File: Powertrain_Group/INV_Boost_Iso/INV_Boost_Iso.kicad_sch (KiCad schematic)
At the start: 16 parts, among them J1 15230682601000, U27 TPS22917DBV

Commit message: [INV_Bost_Isense] V1.1
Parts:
- C41, C42, C43, C44, C45, C46: footprint Personal:C_8060_Murata_DK1 -> nturt_kicad_lib_EP7:C_8060_Murata_DK1
- J1: footprint Samacsys:15230682601000 -> nturt_kicad_lib_EP7:HARTING 15230682601000; symbol Samacsys:15230682601000 -> nturt_kicad_lib_EP7:Harting_15230682601000
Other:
- note added: "V1.0 init by Shinkansen942 V1.1 minor modify by Jack Kuo"
- company: (none) -> NTURacing
- title: (none) -> INV_Boost_Iso
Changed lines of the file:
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@@
 	(generator_version "9.0")
 	(paper "A4")
+	(title_block
+		(title "INV_Boost_Iso")
+		(date "2026-03-06")
+		(rev "1.1")
+		(company "NTURacing")
+		(comment 1 "Shinkansen942")
+		(comment 2 "Jack Kuo")
+	)
+	(text "V1.0 init by Shinkansen942\nV1.1 minor modify by Jack Kuo"
+		(exclude_from_sim no)
+		(at 192.786 92.71 0)
+		(effects
+			(font
+				(size 1.27 1.27)
+			)
+			(justify left top)
+		)
+	)
 	(junction
 		(at 104.14 73.66)
@@
 	)
 	(junction
-		(at 115.57 142.24)
+		(at 121.92 29.21)
 		(diameter 0)
 		(color 0 0 0 0)
 	)
 	(junction
-		(at 121.92 29.21)
+		(at 111.76 139.7)
 		(diameter 0)
 		(color 0 0 0 0)
@@
 	)
 	(junction
-		(at 140.97 134.62)
+		(at 109.22 60.96)
 		(diameter 0)
 		(color 0 0 0 0)
 	)
 	(junction
-		(at 109.22 60.96)
+		(at 48.26 53.34)
 		(diameter 0)
 		(color 0 0 0 0)
 	)
 	(junction
-		(at 48.26 53.34)
+		(at 158.75 73.66)
 		(diameter 0)
 		(color 0 0 0 0)
 	)
 	(junction
-		(at 158.75 73.66)
+		(at 111.76 142.24)
 		(diameter 0)
 		(color 0 0 0 0)
@@
 	)
 	(junction
-		(at 153.67 66.04)
+		(at 143.51 132.08)
 		(diameter 0)
 		(color 0 0 0 0)
 	)
 	(junction
-		(at 140.97 139.7)
+		(at 153.67 66.04)
 		(diameter 0)
 		(color 0 0 0 0)
 	)
 	(junction
-		(at 109.22 63.5)
+		(at 143.51 137.16)
 		(diameter 0)
 		(color 0 0 0 0)
 	)
 	(junction
-		(at 109.22 66.04)
+		(at 143.51 134.62)
 		(diameter 0)
 		(color 0 0 0 0)
 	)
 	(junction
-		(at 140.97 137.16)
+		(at 109.22 63.5)
 		(diameter 0)
 		(color 0 0 0 0)
 	)
 	(junction
-		(at 115.57 139.7)
+		(at 143.51 139.7)
 		(diameter 0)
 		(color 0 0 0 0)
 	)
 	(junction
-		(at 153.67 60.96)
+		(at 109.22 66.04)
 		(diameter 0)
 		(color 0 0 0 0)
 	)
 	(junction
-		(at 140.97 132.08)
+		(at 153.67 60.96)
 		(diameter 0)
 		(color 0 0 0 0)
@@
 	(wire
 		(pts
-			(xy 82.55 29.21) (xy 99.06 29.21)
+			(xy 143.51 139.7) (xy 140.97 139.7)
 		)
 		(stroke
@@
 	(wire
 		(pts
-			(xy 115.57 139.7) (xy 115.57 142.24)
+			(xy 82.55 29.21) (xy 99.06 29.21)
 		)
 		(stroke
@@
 	(wire
 		(pts
-			(xy 104.14 73.66) (xy 115.57 73.66)
+			(xy 143.51 134.62) (xy 143.51 137.16)
 		)
 		(stroke
@@
 	(wire
 		(pts
-			(xy 115.57 137.16) (xy 115.57 139.7)
+			(xy 104.14 73.66) (xy 115.57 73.66)
 		)
 		(stroke
@@
 	(wire
 		(pts
-			(xy 109.22 63.5) (xy 109.22 66.04)
+			(xy 111.76 137.16) (xy 111.76 139.7)
 		)
 		(stroke
@@
 	(wire
 		(pts
-			(xy 48.26 53.34) (xy 60.96 53.34)
+			(xy 109.22 63.5) (xy 109.22 66.04)
 		)
 		(stroke
@@
 	(wire
 		(pts
-			(xy 140.97 139.7) (xy 140.97 142.24)
+			(xy 48.26 53.34) (xy 60.96 53.34)
 		)
 		(stroke
@@
 	(wire
 		(pts
-			(xy 140.97 132.08) (xy 140.97 134.62)
+			(xy 143.51 132.08) (xy 143.51 134.62)
 		)
 		(stroke
@@
 	(wire
 		(pts
+			(xy 111.76 137.16) (xy 115.57 137.16)
+		)
+		(stroke
+			(width 0)
+			(type default)
+		)
+	)
+	(wire
+		(pts
 			(xy 104.14 76.2) (xy 104.14 73.66)
 		)
@@
 	(wire
 		(pts
-			(xy 140.97 137.16) (xy 140.97 139.7)
+			(xy 143.51 137.16) (xy 140.97 137.16)
 		)
 		(stroke
@@
 	(wire
 		(pts
+			(xy 143.51 132.08) (xy 140.97 132.08)
+		)
+		(stroke
+			(width 0)
+			(type default)
+		)
+	)
+	(wire
+		(pts
 			(xy 140.97 73.66) (xy 158.75 73.66)
 		)
@@
 	(wire
 		(pts
+			(xy 143.51 134.62) (xy 140.97 134.62)
+		)
+		(stroke
+			(width 0)
+			(type default)
+		)
+	)
+	(wire
+		(pts
 			(xy 153.67 60.96) (xy 153.67 63.5)
 		)
@@
 	(wire
 		(pts
+			(xy 111.76 142.24) (xy 115.57 142.24)
+		)
+		(stroke
+			(width 0)
+			(type default)
+		)
+	)
+	(wire
+		(pts
 			(xy 115.57 66.04) (xy 109.22 66.04)
 		)
@@
 	(wire
 		(pts
-			(xy 140.97 134.62) (xy 140.97 137.16)
+			(xy 111.76 139.7) (xy 115.57 139.7)
 		)
 		(stroke
@@
 	(wire
 		(pts
-			(xy 149.86 132.08) (xy 140.97 132.08)
+			(xy 143.51 139.7) (xy 143.51 142.24)
+		)
+		(stroke
+			(width 0)
+			(type default)
+		)
+	)
+	(wire
+		(pts
+			(xy 149.86 132.08) (xy 143.51 132.08)
 		)
 		(stroke
@@
 	(wire
 		(pts
+			(xy 111.76 139.7) (xy 111.76 142.24)
+		)
+		(stroke
+			(width 0)
+			(type default)
+		)
+	)
+	(wire
+		(pts
 			(xy 107.95 71.12) (xy 115.57 71.12)
 		)
@@
 	(wire
 		(pts
-			(xy 105.41 142.24) (xy 115.57 142.24)
+			(xy 105.41 142.24) (xy 111.76 142.24)
+		)
+		(stroke
+			(width 0)
+			(type default)
+		)
+	)
+	(wire
+		(pts
+			(xy 143.51 142.24) (xy 140.97 142.24)
 		)
 		(stroke
@@
 		)
 	)
+	(wire
+		(pts
+			(xy 143.51 137.16) (xy 143.51 139.7)
+		)
+		(stroke
+			(width 0)
+			(type default)
+		)
+	)
 	(label "V1P"
 		(at 115.57 129.54 180)
@@
 			)
 		)
-		(property "Footprint" "Personal:C_8060_Murata_DK1"
+		(property "Footprint" "nturt_kicad_lib_EP7:C_8060_Murata_DK1"
 			(at 120.9548 21.59 0)
 			(effects
@@
 			)
 		)
-		(property "Footprint" "Personal:C_8060_Murata_DK1"
+		(property "Footprint" "nturt_kicad_lib_EP7:C_8060_Murata_DK1"
 			(at 164.1348 21.59 0)
 			(effects
@@
 			)
 		)
-		(property "Footprint" "Personal:C_8060_Murata_DK1"
+		(property "Footprint" "nturt_kicad_lib_EP7:C_8060_Murata_DK1"
 			(at 73.9648 21.59 0)
 			(effects
@@
 			)
 		)
-		(property "Footprint" "Personal:C_8060_Murata_DK1"
+		(property "Footprint" "nturt_kicad_lib_EP7:C_8060_Murata_DK1"
 			(at 98.0948 21.59 0)
 			(effects
@@
 			)
 		)
-		(property "Footprint" "Personal:C_8060_Murata_DK1"
+		(property "Footprint" "nturt_kicad_lib_EP7:C_8060_Murata_DK1"
 			(at 185.7248 21.59 0)
 			(effects
@@
 			)
 		)
-		(property "Footprint" "Personal:C_8060_Murata_DK1"
+		(property "Footprint" "nturt_kicad_lib_EP7:C_8060_Murata_DK1"
 			(at 142.5448 21.59 0)
 			(effects
@@
 	)
 	(symbol
-		(lib_id "Samacsys:15230682601000")
+		(lib_id "nturt_kicad_lib_EP7:Harting_15230682601000")
 		(at 115.57 58.42 0)
 		(unit 1)
@@
 			)
 		)
-		(property "Footprint" "Samacsys:15230682601000"
+		(property "Footprint" "nturt_kicad_lib_EP7:HARTING 15230682601000"
 			(at 137.16 153.34 0)
 			(effects
@@
 		)
 		(instances
-			(project "Boost_Iso"
+			(project "INV_Boost_Iso"
 				(path "/75ceed66-07fe-423e-80e3-45d976fe7c9f"
 					(page "3")
@@
 		)
 		(instances
-			(project "Boost_Iso"
+			(project "INV_Boost_Iso"
 				(path "/75ceed66-07fe-423e-80e3-45d976fe7c9f"
 					(page "2")
@@
 		)
 		(instances
-			(project "Boost_Iso"
+			(project "INV_Boost_Iso"
 				(path "/75ceed66-07fe-423e-80e3-45d976fe7c9f"
 					(page "9")
@@
 		)
 		(instances
-			(project "Boost_Iso"
+			(project "INV_Boost_Iso"
 				(path "/75ceed66-07fe-423e-80e3-45d976fe7c9f"
 					(page "6")
@@
 		)
 		(instances
-			(project "Boost_Iso"
+			(project "INV_Boost_Iso"
 				(path "/75ceed66-07fe-423e-80e3-45d976fe7c9f"
 					(page "8")
@@
 		)
 		(instances
-			(project "Boost_Iso"
+			(project "INV_Boost_Iso"
 				(path "/75ceed66-07fe-423e-80e3-45d976fe7c9f"
 					(page "4")
@@
 		)
 		(instances
-			(project "Boost_Iso"
+			(project "INV_Boost_Iso"
 				(path "/75ceed66-07fe-423e-80e3-45d976fe7c9f"
 					(page "7")
@@
 		)
 		(instances
-			(project "Boost_Iso"
+			(project "INV_Boost_Iso"
 				(path "/75ceed66-07fe-423e-80e3-45d976fe7c9f"
 					(page "5")

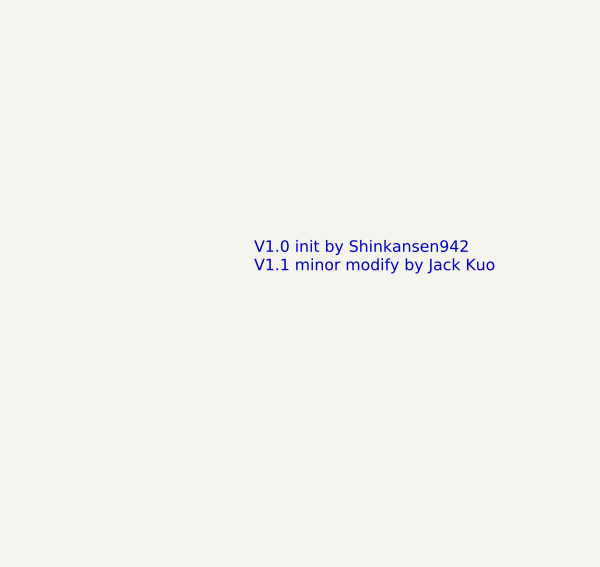
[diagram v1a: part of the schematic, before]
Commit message: [INV_Boost_Iso] V1.2
swap 0402 with 0603
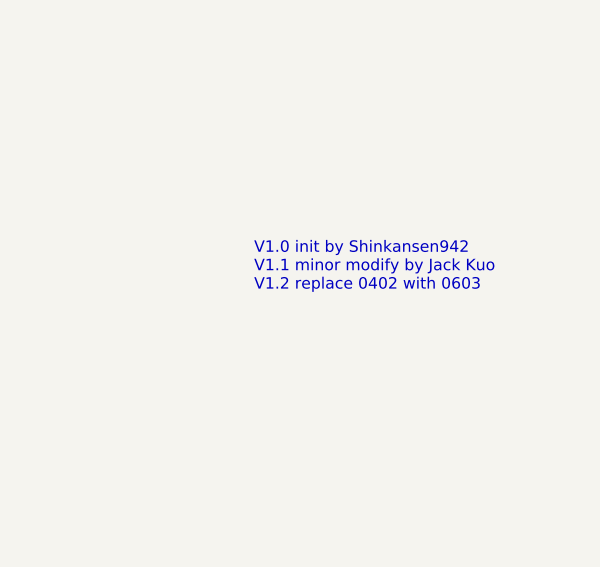
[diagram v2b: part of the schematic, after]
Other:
- note added: "V1.0 init by Shinkansen942 V1.1 minor modify by Jack Kuo V1.2 replace 0402 with 0603"
- note removed: "V1.0 init by Shinkansen942 V1.1 minor modify by Jack Kuo"
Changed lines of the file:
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@@
 	(title_block
 		(title "INV_Boost_Iso")
-		(date "2026-03-06")
-		(rev "1.1")
+		(date "2026-03-09")
+		(rev "1.2")
 		(company "NTURacing")
 		(comment 1 "Shinkansen942")
 		(comment 2 "Jack Kuo")
 	)
-	(text "V1.0 init by Shinkansen942\nV1.1 minor modify by Jack Kuo"
+	(text "V1.0 init by Shinkansen942\nV1.1 minor modify by Jack Kuo\nV1.2 replace 0402 with 0603"
 		(exclude_from_sim no)
 		(at 192.786 92.71 0)
